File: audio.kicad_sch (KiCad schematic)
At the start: 38 parts, among them J1 SJ-43515RS-SMT-TR, J2 SJ-43515RS-SMT-TR, U6 PCM5122PW, U7 OPA1622, X1 ASE-45.1584MHz, X2 ASE-24.576MHz

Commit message: pcb / inital work
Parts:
- added C19, C20: 0.1uF, Capacitor_SMD:C_0805_2012Metric, symbol PCM_SL_Devices:Capacitor_NP
- added C48, C49: 22uF, Capacitor_SMD:C_0805_2012Metric, symbol PCM_SL_Devices:Capacitor_NP
- added D5, D6, D7, D8: SP1005-01WTG, PCM_Diode_SMD_AKL:D_0201_0603Metric, symbol PCM_Diode_TVS_AKL:SP1005-01WTG
- added R41, R42: 0, Resistor_SMD:R_0603_1608Metric, symbol PCM_Elektuur:R
- added U14: OPA1622, Package_SON:Texas_S-PVSON-N10, symbol Amplifier_Audio:OPA1622
- C11, C12, C4, C5: footprint Capacitor_THT:C_Disc_D3.0mm_W2.0mm_P2.50mm -> Capacitor_SMD:C_0402_1005Metric
- C25, C26, C32, C34, C36, C39, C46, C47: footprint Capacitor_THT:C_Disc_D3.0mm_W2.0mm_P2.50mm -> Capacitor_SMD:C_0805_2012Metric
- C33, C35, C37, C38, C40: footprint Capacitor_THT:CP_Radial_D5.0mm_P2.50mm -> Capacitor_Tantalum_SMD:CP_EIA-3528-21_Kemet-B
- J1: now fitted
- R11, R12, R29, R30, R31, R32, R33, R38, R39, R5, R6: footprint (none) -> Resistor_SMD:R_0603_1608Metric
- R14, R15: value 10 -> 100; footprint (none) -> Resistor_SMD:R_0603_1608Metric; now fitted
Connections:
- net AGND: now also C19.1, C20.1, C48.1, C49.1, D5.2 (A), D6.2 (A), D7.2 (A), D8.2 (A), U14.3 (GND)
- net V3.3_ANA: now also U14.8 (EN)
- net V5N_ANA: now also C20.2, C49.2, U14.11 (V-), U14.4 (V-)
- net V5P_ANA: now also C19.2, C48.2, U14.2 (V+)
- net FILTERED_R: now reaches C5.2, R12.2 (-), R29.1 (+), U7.5 (+)
- net FILTERED_R: now also U14.1 (+)
- net at J1.2, R14.2 (-): now also D8.1 (K)
- net at J1.3, R15.2 (-): now also D7.1 (K)
- net FILTERED_L: now reaches C4.2, R11.2 (-), R32.1 (+), U7.1 (+)
- net FILTERED_L: now also U14.5 (+)
- net at J2.2, R30.2 (-): now also D6.1 (K)
- net at J2.3, R31.2 (-): now also D5.1 (K)
- net JACK_LINE_L renamed LINEOUT_L
- net LINEOUT_L: now also R41.2 (-), U14.7
- net JACK_LINE_R renamed LINEOUT_R
- net LINEOUT_R: now also R42.2 (-), U14.9
- new net: R42.1 (+), U14.10 (-)
- new net: R41.1 (+), U14.6 (-)
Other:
- moved on the sheet: R30, R31

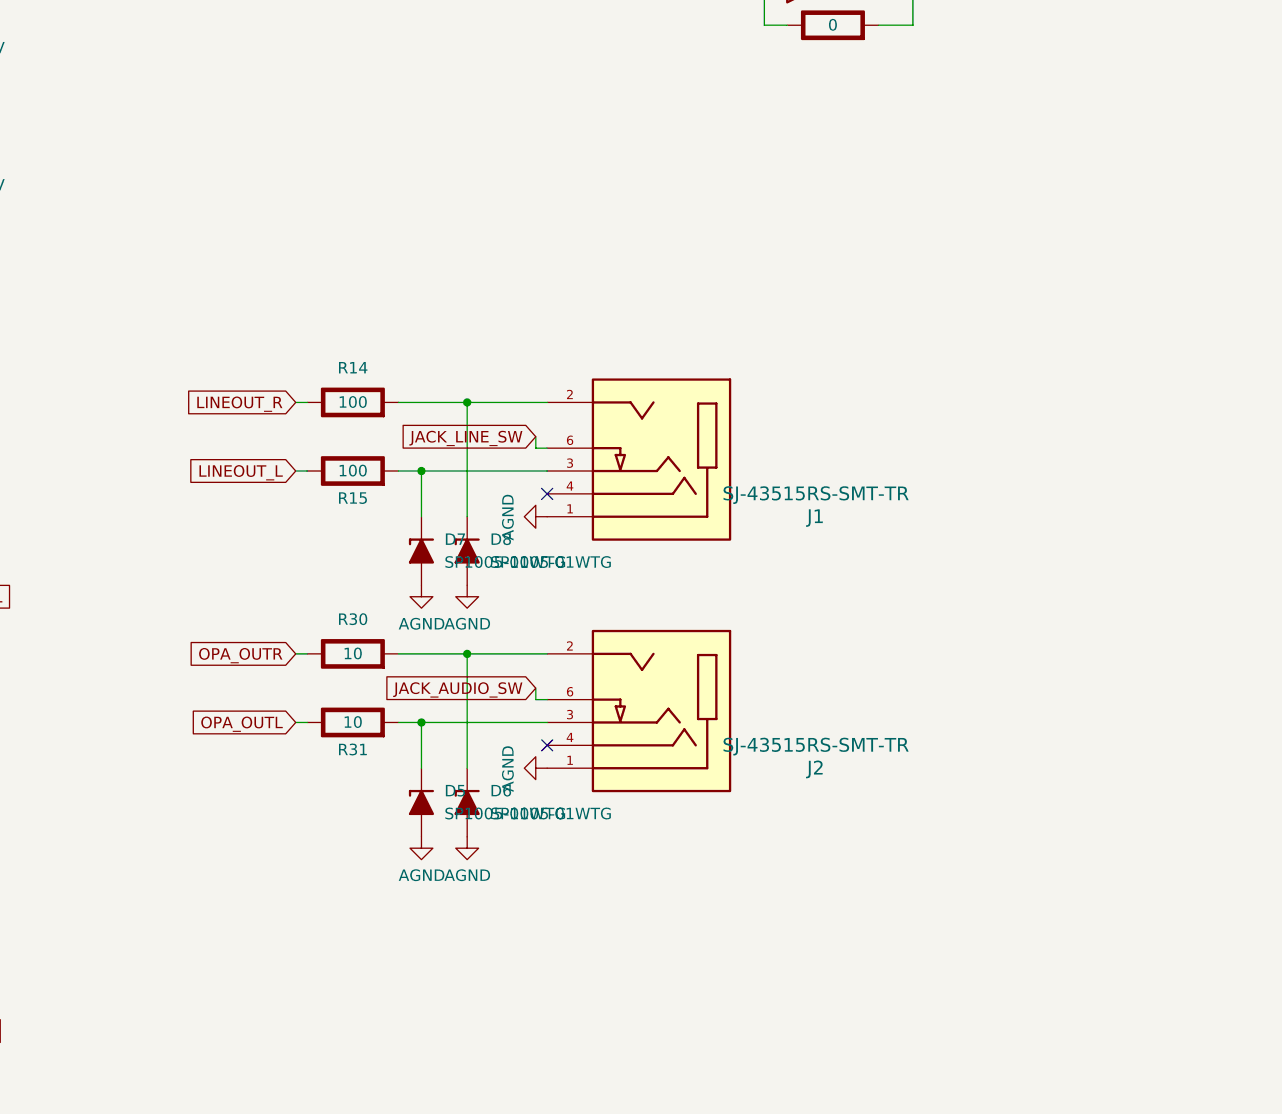
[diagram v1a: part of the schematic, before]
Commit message: ICs placed
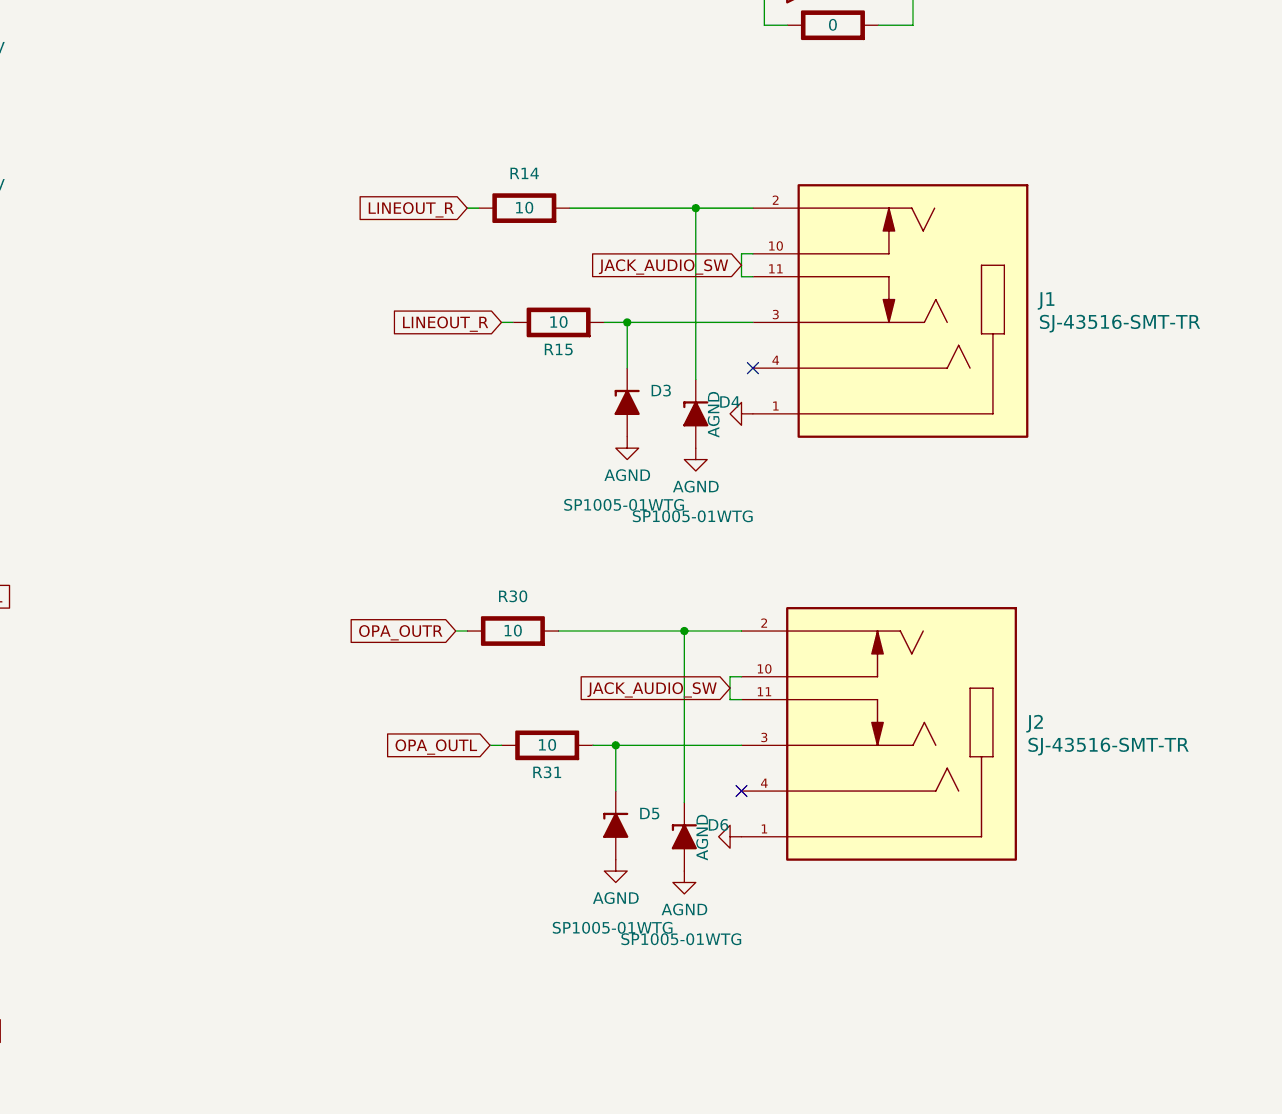
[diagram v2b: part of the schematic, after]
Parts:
- removed D7, D8: SP1005-01WTG, PCM_Diode_SMD_AKL:D_0201_0603Metric, symbol PCM_Diode_TVS_AKL:SP1005-01WTG
- added D3, D4: SP1005-01WTG, PCM_Diode_SMD_AKL:D_0201_0603Metric, symbol PCM_Diode_TVS_AKL:SP1005-01WTG
- J1, J2: value SJ-43515RS-SMT-TR -> SJ-43516-SMT-TR; footprint CUI_SJ-43515RS-SMT-TR -> uwu:CUI_SJ2-35894D-SMT-TR; symbol uwu:SJ-43515RS-SMT-TR -> uwu:SJ2-35894D-SMT-TR; MAXIMUM_PACKAGE_HEIGHT 5.3mm -> 5.2 mm; PARTREV 1.05 -> 1.04
- R14, R15: value 100 -> 10
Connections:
- net AGND: now also D3.2 (A), D4.2 (A)
- net JACK_AUDIO_SW: now also J1.10, J1.11, J2.10, J2.11; no longer J2.6
- net LINEOUT_L: no longer R15.1 (+)
- net LINEOUT_R: now also R15.1 (+)
- net at J1.2, R14.2 (-): now also D4.1 (K)
- net at J1.3, R15.2 (-): now also D3.1 (K)
- removed net JACK_LINE_SW: J1.6
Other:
- moved on the sheet: D5, D6, R30, R31

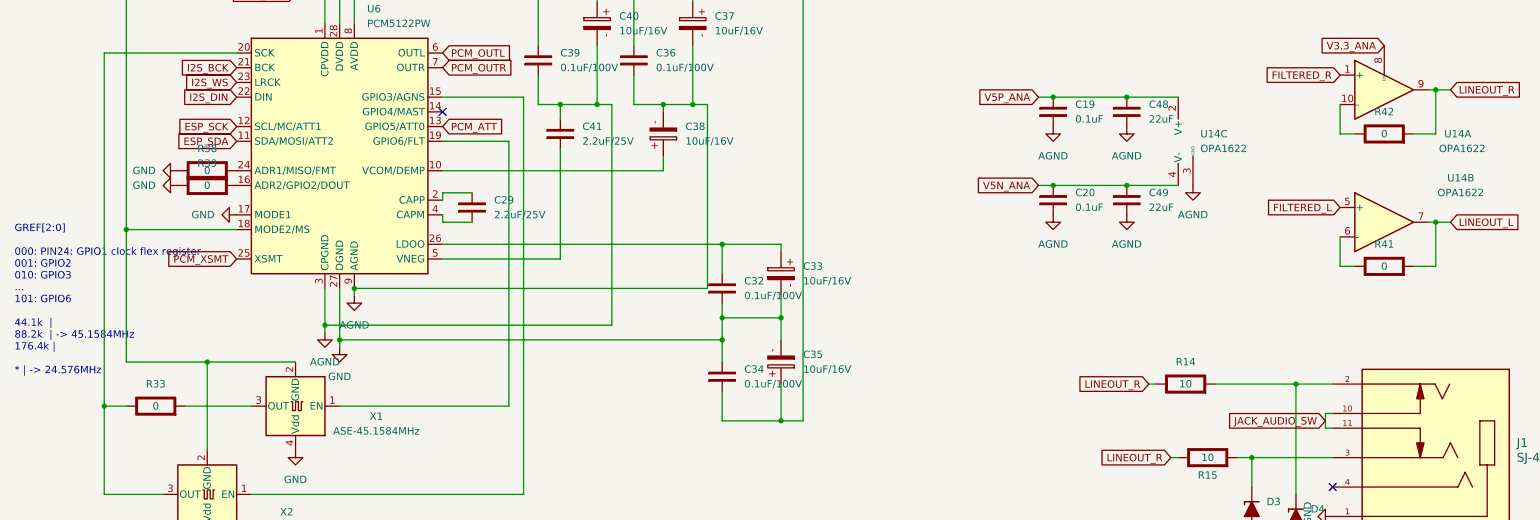
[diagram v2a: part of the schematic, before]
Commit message: all pcb elements positioned + minor schematics changes
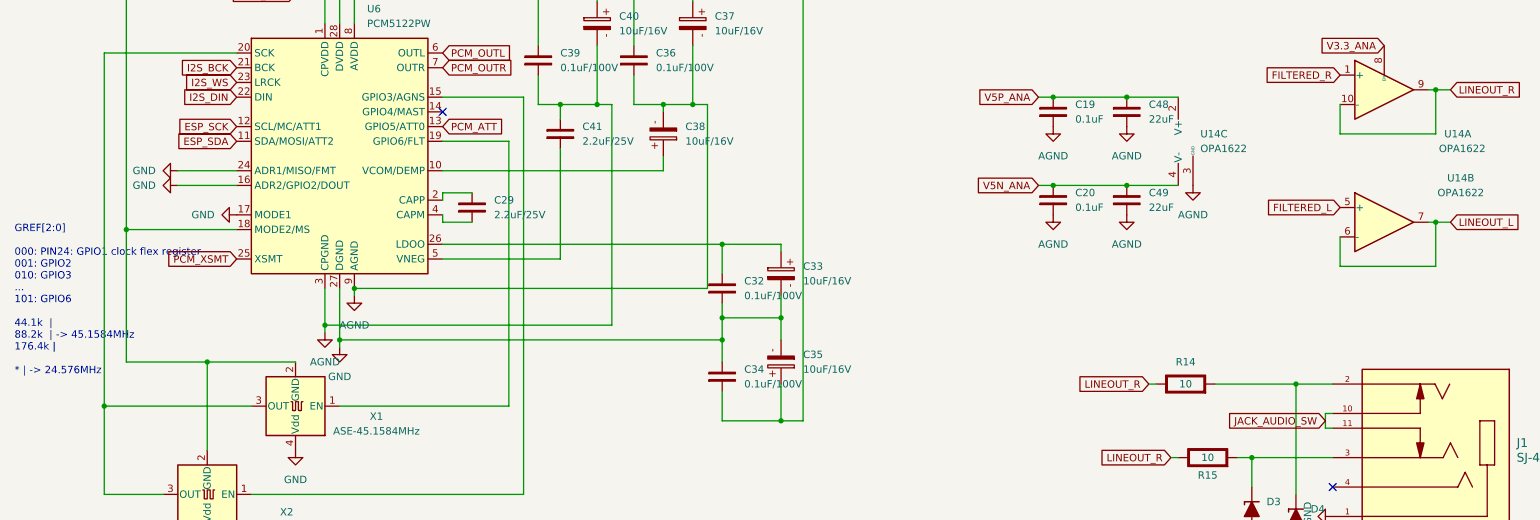
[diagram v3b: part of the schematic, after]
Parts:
- removed R33, R38, R39, R41, R42: 0, Resistor_SMD:R_0603_1608Metric, symbol PCM_Elektuur:R
- C29, C41: footprint Capacitor_THT:C_Disc_D3.0mm_W2.0mm_P2.50mm -> Capacitor_SMD:C_0603_1608Metric
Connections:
- net GND: now also U6.16 (ADR2/GPIO2/DOUT), U6.24 (ADR1/MISO/FMT)
- net LINEOUT_L: now also U14.6 (-)
- net LINEOUT_R: now also U14.10 (-)
- net at U6.20 (SCK), X2.3 (OUT): now also X1.3 (OUT)

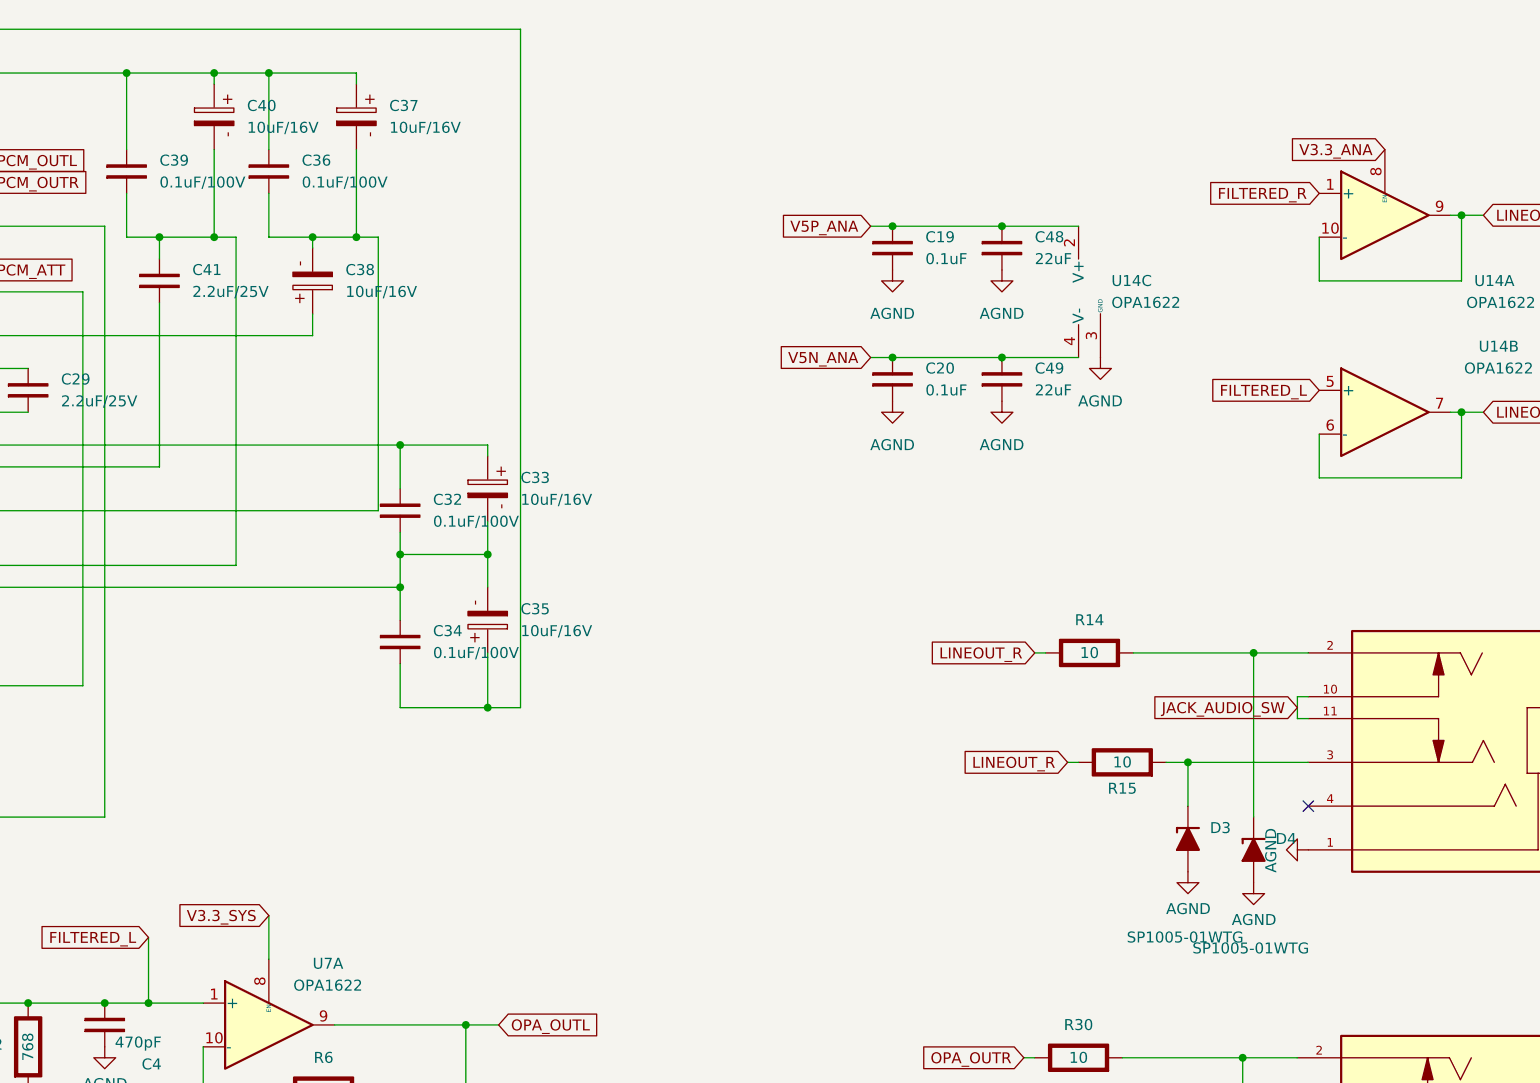
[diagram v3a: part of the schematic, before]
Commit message: changing ic placement
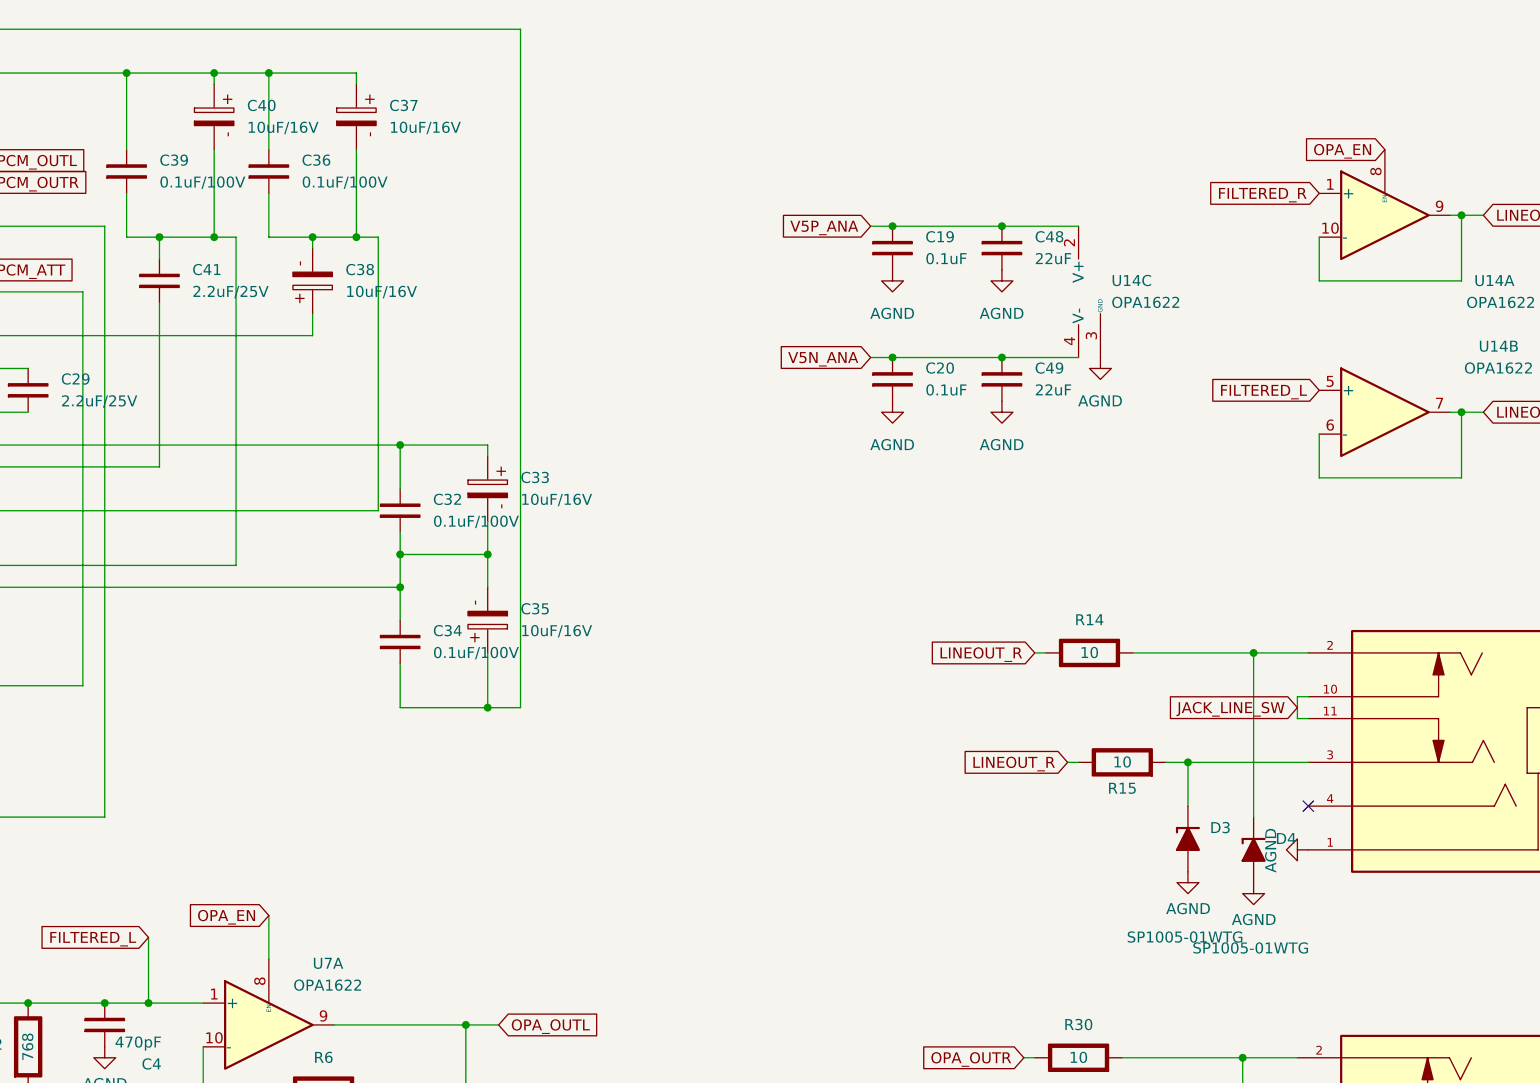
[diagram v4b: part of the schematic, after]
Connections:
- net JACK_AUDIO_SW: no longer J1.10, J1.11
- net V3.3_ANA: no longer U14.8 (EN)
- net V3.3_SYS: no longer U7.8 (EN)
- new net JACK_LINE_SW: J1.10, J1.11
- new net OPA_EN: U14.8 (EN), U7.8 (EN)

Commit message: routing
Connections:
- net OPA_EN renamed JACK_EN
- net JACK_EN: no longer U14.8 (EN)
- new net LINEOUT_EN: U14.8 (EN)
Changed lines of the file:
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@@
 		)
 	)
-	(global_label "OPA_EN"
+	(global_label "JACK_EN"
 		(shape input)
 		(at 121.92 118.11 180)
@@
 		)
 		(property "Intersheetrefs" "${INTERSHEET_REFS}"
-			(at 111.7986 118.11 0)
+			(at 110.8915 118.11 0)
 			(effects
 				(font
@@
 		)
 	)
-	(global_label "OPA_EN"
+	(global_label "LINEOUT_EN"
 		(shape input)
 		(at 251.46 29.21 180)
@@
 		)
 		(property "Intersheetrefs" "${INTERSHEET_REFS}"
-			(at 241.3386 29.21 0)
+			(at 237.2867 29.21 0)
 			(effects
 				(font
